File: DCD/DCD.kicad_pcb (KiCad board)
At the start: 4 copper layers, 110 x 110 mm, 172 parts, among them IC1 830S21AMI-01LF, IC2 830S21AMI-01LF, J1 UMPS-04-03.5-G-VT-SM-WT, J2 UMPS-04-03.5-G-VT-SM-WT, J3 UMPS-04-03.5-G-VT-SM-WT, J4 UMPS-04-03.5-G-VT-SM-WT, J5 Conn_02x04_Top_Bottom, U1 TLV76780DBVR, U10 OPA277UA, U11 DAC8811ICDGKT, U12 DAC8811ICDGKT, U13 OPA277UA, U14 OPA277UA, U15 MC100EP31DTG, U16 MC100EP31DTG, U2 ADP7182AUJZ-1.8-R7, U3 LP2985-50DBVR, U4 LP2985-18DBVR, U5 LP2985-33DBVR, U6 ADR4550BRZ, U7 LP2985-33DBVR, U8 CDCLVC1104PWR, U9 AD4630-24BBCZ, Y1 SiT8208AI-21-33E-50.000000

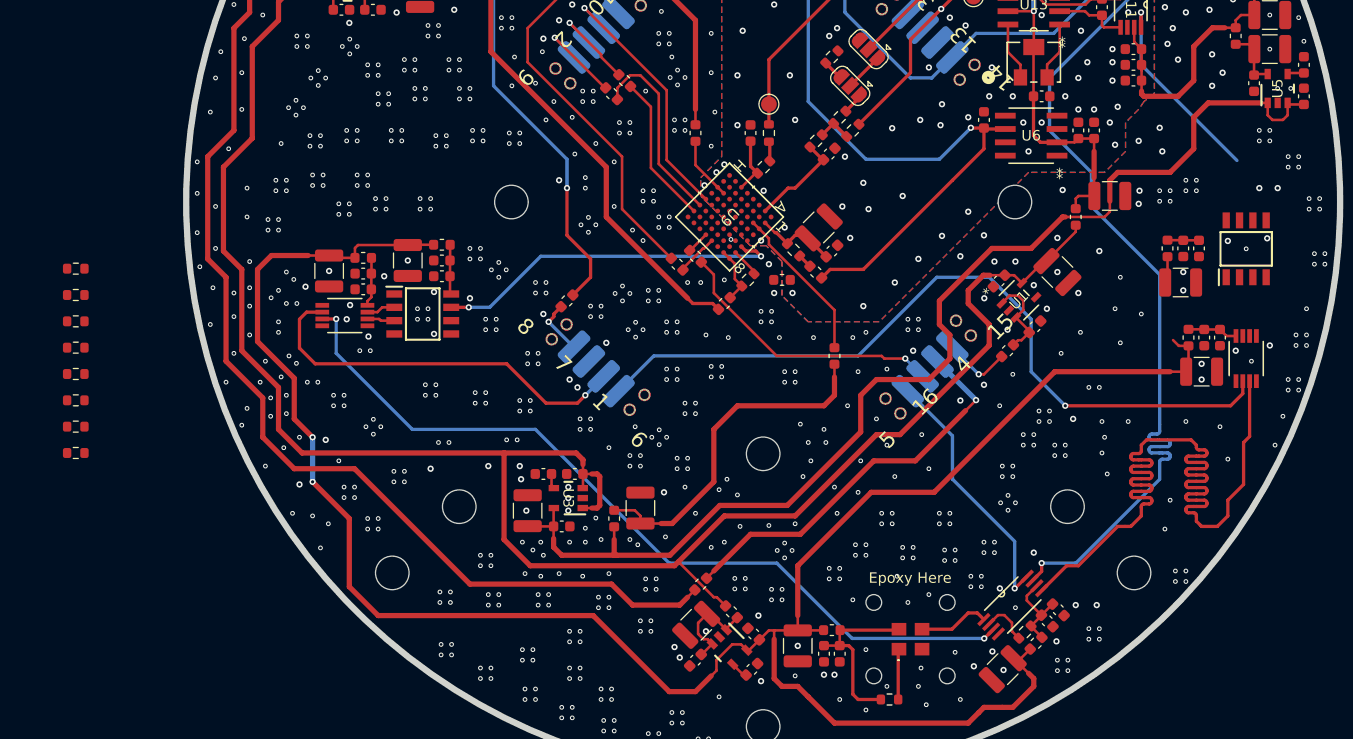
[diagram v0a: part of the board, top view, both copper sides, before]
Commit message: Added components part numbers and stuff. Added termination resistors
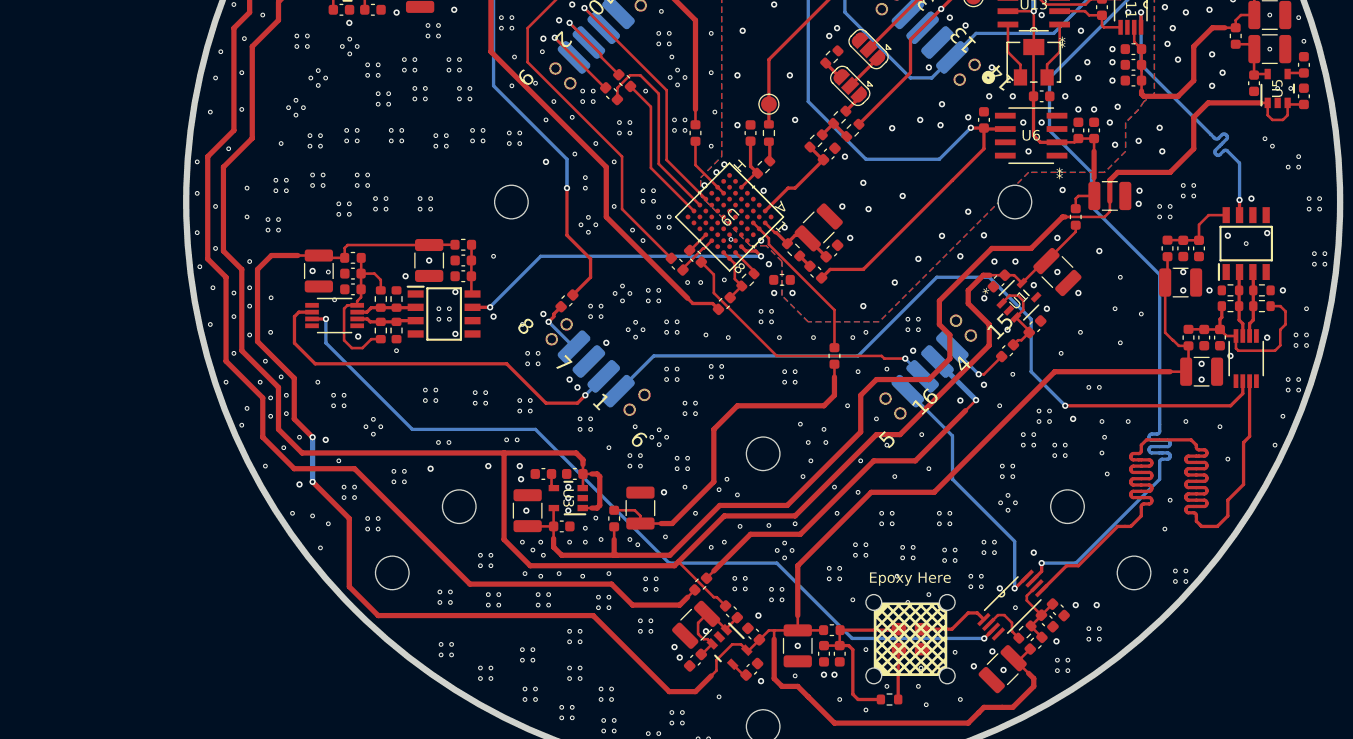
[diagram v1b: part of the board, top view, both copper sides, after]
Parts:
- moved R6 113.1 mm to (194.2, 105.0)
- moved R7 113.1 mm to (194.2, 103.5), turned to 180 degrees
- moved R9 110.2 mm to (191.2, 103.5)
- moved R8 110.1 mm to (191.2, 105.0), turned to 180 degrees
- moved R22 33.9 mm to (111.8, 104.3), turned to -90 degrees
- moved R21 31.5 mm to (110.2, 104.3), turned to 90 degrees
- moved R13 31.3 mm to (111.8, 107.3), turned to 90 degrees
- moved R12 29.4 mm to (110.2, 107.3), turned to -90 degrees
- moved C67 2.04 mm to (118.1, 102.2)
- moved C68 2.04 mm to (118.1, 100.7)
- moved C69 2.04 mm to (114.9, 100.7)
- moved FB29 2.04 mm to (118.1, 99.2)
- moved IC2 2.04 mm to (116.3, 105.8)
- moved C64 0.98 mm to (104.3, 101.7)
- moved C65 0.98 mm to (107.6, 101.9)
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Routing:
- net Net-(U15-VCC): track 4.79 -> 17.9 mm
- net Net-(U16-VCC): track 4.68 -> 16.4 mm
- net /Comms/*CS1: track 19.3 -> 28.0 mm
- net 3V3_CLK: track 200.8 -> 208.7 mm
- net Net-(IC1-NCLK): track 0.08 -> 6.34 mm
- net Net-(IC1-CLK): track 0.00 -> 6.26 mm
- net Net-(IC1-VDD): track 3.27 -> 7.72 mm
- net Net-(IC2-NCLK): track 2.63 -> 5.74 mm
- net Net-(IC2-CLK): track 2.75 -> 5.77 mm
- net /ADC/CNV: track 33.8 -> 31.8 mm
- net /ADC/DGND: vias 945 -> 918

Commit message: Component placement
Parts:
- removed B1: DIN933 M3x14mm, custom_components:Screw_DIN933_M3x14mm
- removed C38: 1µF, Capacitor_SMD:C_0603_1608Metric
- removed C40: 100p, Capacitor_SMD:C_0603_1608Metric
- removed C43: 1nF, Capacitor_SMD:C_0603_1608Metric
- removed C44: 10pF, Capacitor_SMD:C_0603_1608Metric
- removed C47, C48: 100nF, Capacitor_SMD:C_0603_1608Metric
- removed FB11, FB12, FB14: 470Ω, Inductor_SMD:L_0603_1608Metric
- removed H1, H10, H11, H12, H13, H14, H2, H3, H4, H5, H6, H7, H8, H9: M3 Mounting hole, LOBSTER:MountingHole_3.2mm_M3_NoMask
- removed H15: Spacer M3x5mm, custom_components:ThreadedSpacer_6mm_M3x0.5_5mm
- removed J1, J2, J3, J4: UMPS-04-03.5-G-VT-SM-WT, custom_components:UMPS-04-03.5-G-VT-SM-WT
- removed J5: Conn_02x04_Top_Bottom, Connector_PinHeader_2.54mm:PinHeader_2x04_P2.54mm_Vertical
- removed JP1, JP2: SolderJumper_3_Open, Jumper:SolderJumper-3_P1.3mm_Open_RoundedPad1.0x1.5mm
- removed N1, N2, N3, N4, N5, N6, N7: M3 Thumbnut, custom_components:ThumbNut-M3
- removed R17: 47, Resistor_SMD:R_0603_1608Metric
- removed R18, R19, R20: 1k, Resistor_SMD:R_0603_1608Metric
- removed R3, R4, R5: 10k, Resistor_SMD:R_0603_1608Metric
- removed RV1, RV2, RV3: 20kR, custom_components:IC3_3214W-1-203E_BRN
- removed TP1, TP2: TestPoint, TestPoint:TestPoint_Pad_D1.5mm
- removed U11: DAC8811ICDGKT, custom_components:DGK8
- removed U13: OPA277UA, custom_components:D8
- added C23: 10uF, Capacitor_SMD:C_1210_3225Metric, F.Cu at (194.5, 47.6)
- added C23: 10uF, Capacitor_SMD:C_1210_3225Metric, F.Cu at (138.7, 78.9)
- added C23: 10uF, Capacitor_SMD:C_1210_3225Metric, F.Cu at (122.5, 46.9)
- added C23: 10uF, Capacitor_SMD:C_1210_3225Metric, F.Cu at (152.9, 79.4)
- added C23: 10uF, Capacitor_SMD:C_1210_3225Metric, F.Cu at (123.7, 77.9)
- added C23: 10uF, Capacitor_SMD:C_1210_3225Metric, F.Cu at (107.9, 79.2)
- added C23: 10uF, Capacitor_SMD:C_1210_3225Metric, F.Cu at (90.9, 79.4)
- added C23: 10uF, Capacitor_SMD:C_1210_3225Metric, F.Cu at (180.5, 47.9)
- added C23: 10uF, Capacitor_SMD:C_1210_3225Metric, F.Cu at (137.3, 46.9)
- added C23: 10uF, Capacitor_SMD:C_1210_3225Metric, F.Cu at (167.2, 79.7)
- added C23: 10uF, Capacitor_SMD:C_1210_3225Metric, F.Cu at (181.9, 79.7)
- added C23: 10uF, Capacitor_SMD:C_1210_3225Metric, F.Cu at (196.2, 79.7)
- added C23: 10uF, Capacitor_SMD:C_1210_3225Metric, F.Cu at (107.3, 46.4)
- added C23: 10uF, Capacitor_SMD:C_1210_3225Metric, F.Cu at (166.0, 47.6)
- added C23: 10uF, Capacitor_SMD:C_1210_3225Metric, F.Cu at (151.5, 47.9)
- added C30: 10uF, Capacitor_SMD:C_1210_3225Metric, B.Cu at (129.0, 51.5)
- added C30: 10uF, Capacitor_SMD:C_1210_3225Metric, B.Cu at (129.7, 21.9)
- added C30: 10uF, Capacitor_SMD:C_1210_3225Metric, B.Cu at (102.0, 22.7)
- added C30: 10uF, Capacitor_SMD:C_1210_3225Metric, B.Cu at (156.5, 21.4)
- added C30: 10uF, Capacitor_SMD:C_1210_3225Metric, B.Cu at (102.0, 52.0)
- added C30: 10uF, Capacitor_SMD:C_1210_3225Metric, B.Cu at (156.7, 50.0)
- added C30: 10uF, Capacitor_SMD:C_1210_3225Metric, B.Cu at (182.7, 49.0)
- added C32: 100nF, Capacitor_SMD:C_0603_1608Metric, B.Cu at (180.3, 49.8)
- added C32: 100nF, Capacitor_SMD:C_0603_1608Metric, B.Cu at (154.3, 50.8)
- added C32: 100nF, Capacitor_SMD:C_0603_1608Metric, B.Cu at (99.5, 52.8)
- added C32: 100nF, Capacitor_SMD:C_0603_1608Metric, B.Cu at (154.0, 22.2)
- added C32: 100nF, Capacitor_SMD:C_0603_1608Metric, B.Cu at (126.5, 52.2)
- added C32: 100nF, Capacitor_SMD:C_0603_1608Metric, B.Cu at (99.5, 23.4)
- added C32: 100nF, Capacitor_SMD:C_0603_1608Metric, B.Cu at (127.3, 22.7)
- added C36: 1nF, Capacitor_SMD:C_0603_1608Metric, B.Cu at (160.7, 19.7)
- added C36: 1nF, Capacitor_SMD:C_0603_1608Metric, B.Cu at (161.0, 48.3)
- added C36: 1nF, Capacitor_SMD:C_0603_1608Metric, B.Cu at (187.0, 47.3)
- added C36: 1nF, Capacitor_SMD:C_0603_1608Metric, B.Cu at (106.2, 50.3)
- added C36: 1nF, Capacitor_SMD:C_0603_1608Metric, B.Cu at (133.2, 49.8)
- added C36: 1nF, Capacitor_SMD:C_0603_1608Metric, B.Cu at (106.2, 20.9)
- added C36: 1nF, Capacitor_SMD:C_0603_1608Metric, B.Cu at (134.0, 20.2)
- added C37: 1nF, Capacitor_SMD:C_0603_1608Metric, B.Cu at (140.7, 20.2)
- added C37: 1nF, Capacitor_SMD:C_0603_1608Metric, B.Cu at (167.4, 19.7)
- added C37: 1nF, Capacitor_SMD:C_0603_1608Metric, B.Cu at (112.9, 50.3)
- added C37: 1nF, Capacitor_SMD:C_0603_1608Metric, B.Cu at (167.7, 48.3)
- added C37: 1nF, Capacitor_SMD:C_0603_1608Metric, B.Cu at (139.9, 49.8)
- added C37: 1nF, Capacitor_SMD:C_0603_1608Metric, B.Cu at (112.9, 20.9)
- added C37: 1nF, Capacitor_SMD:C_0603_1608Metric, B.Cu at (193.7, 47.3)
- added C39: 1µF, Capacitor_SMD:C_0603_1608Metric, F.Cu at (201.2, 62.8)
- added C39: 1µF, Capacitor_SMD:C_0603_1608Metric, F.Cu at (112.9, 62.2)
- added C39: 1µF, Capacitor_SMD:C_0603_1608Metric, F.Cu at (156.5, 31.0)
- added C39: 1µF, Capacitor_SMD:C_0603_1608Metric, F.Cu at (95.9, 62.5)
- added C39: 1µF, Capacitor_SMD:C_0603_1608Metric, F.Cu at (143.7, 62.0)
- added C39: 1µF, Capacitor_SMD:C_0603_1608Metric, F.Cu at (127.5, 30.0)
- added C39: 1µF, Capacitor_SMD:C_0603_1608Metric, F.Cu at (157.9, 62.5)
- added C39: 1µF, Capacitor_SMD:C_0603_1608Metric, F.Cu at (172.2, 62.7)
- added C39: 1µF, Capacitor_SMD:C_0603_1608Metric, F.Cu at (128.7, 61.0)
- added C39: 1µF, Capacitor_SMD:C_0603_1608Metric, F.Cu at (171.0, 30.7)
- added C39: 1µF, Capacitor_SMD:C_0603_1608Metric, F.Cu at (112.3, 29.5)
- added C39: 1µF, Capacitor_SMD:C_0603_1608Metric, F.Cu at (199.5, 30.7)
- added C39: 1µF, Capacitor_SMD:C_0603_1608Metric, F.Cu at (142.3, 30.0)
- added C39: 1µF, Capacitor_SMD:C_0603_1608Metric, F.Cu at (186.9, 62.7)
- added C39: 1µF, Capacitor_SMD:C_0603_1608Metric, F.Cu at (185.5, 31.0)
- added C41: 100p, Capacitor_SMD:C_0603_1608Metric, F.Cu at (112.3, 26.5)
- added C41: 100p, Capacitor_SMD:C_0603_1608Metric, F.Cu at (143.7, 59.0)
- added C41: 100p, Capacitor_SMD:C_0603_1608Metric, F.Cu at (142.3, 27.0)
- added C41: 100p, Capacitor_SMD:C_0603_1608Metric, F.Cu at (156.5, 28.0)
- added C41: 100p, Capacitor_SMD:C_0603_1608Metric, F.Cu at (157.9, 59.5)
- added C41: 100p, Capacitor_SMD:C_0603_1608Metric, F.Cu at (128.7, 58.0)
- added C41: 100p, Capacitor_SMD:C_0603_1608Metric, F.Cu at (186.9, 59.7)
- added C41: 100p, Capacitor_SMD:C_0603_1608Metric, F.Cu at (171.0, 27.7)
- added C41: 100p, Capacitor_SMD:C_0603_1608Metric, F.Cu at (112.9, 59.2)
- added C41: 100p, Capacitor_SMD:C_0603_1608Metric, F.Cu at (95.9, 59.5)
- added C41: 100p, Capacitor_SMD:C_0603_1608Metric, F.Cu at (201.2, 59.8)
- added C41: 100p, Capacitor_SMD:C_0603_1608Metric, F.Cu at (172.2, 59.7)
- added C41: 100p, Capacitor_SMD:C_0603_1608Metric, F.Cu at (127.5, 27.0)
- added C41: 100p, Capacitor_SMD:C_0603_1608Metric, F.Cu at (199.5, 27.7)
- added C41: 100p, Capacitor_SMD:C_0603_1608Metric, F.Cu at (185.5, 28.0)
- added C42: 1nF, Capacitor_SMD:C_0603_1608Metric, F.Cu at (199.5, 29.2)
- added C42: 1nF, Capacitor_SMD:C_0603_1608Metric, F.Cu at (128.7, 59.5)
- added C42: 1nF, Capacitor_SMD:C_0603_1608Metric, F.Cu at (185.5, 29.5)
- added C42: 1nF, Capacitor_SMD:C_0603_1608Metric, F.Cu at (95.9, 61.0)
- added C42: 1nF, Capacitor_SMD:C_0603_1608Metric, F.Cu at (201.2, 61.3)
- added C42: 1nF, Capacitor_SMD:C_0603_1608Metric, F.Cu at (143.7, 60.5)
- added C42: 1nF, Capacitor_SMD:C_0603_1608Metric, F.Cu at (112.9, 60.7)
- added C42: 1nF, Capacitor_SMD:C_0603_1608Metric, F.Cu at (172.2, 61.2)
- added C42: 1nF, Capacitor_SMD:C_0603_1608Metric, F.Cu at (171.0, 29.2)
- added C42: 1nF, Capacitor_SMD:C_0603_1608Metric, F.Cu at (157.9, 61.0)
- added C42: 1nF, Capacitor_SMD:C_0603_1608Metric, F.Cu at (156.5, 29.5)
- added C42: 1nF, Capacitor_SMD:C_0603_1608Metric, F.Cu at (142.3, 28.5)
- added C42: 1nF, Capacitor_SMD:C_0603_1608Metric, F.Cu at (127.5, 28.5)
- added C42: 1nF, Capacitor_SMD:C_0603_1608Metric, F.Cu at (112.3, 28.0)
- added C42: 1nF, Capacitor_SMD:C_0603_1608Metric, F.Cu at (186.9, 61.2)
- added C45: 10pF, Capacitor_SMD:C_0603_1608Metric, F.Cu at (196.6, 23.2)
- added C45: 10pF, Capacitor_SMD:C_0603_1608Metric, F.Cu at (109.3, 22.0)
- added C45: 10pF, Capacitor_SMD:C_0603_1608Metric, F.Cu at (124.6, 22.5)
- added C45: 10pF, Capacitor_SMD:C_0603_1608Metric, F.Cu at (125.7, 53.5)
- added C45: 10pF, Capacitor_SMD:C_0603_1608Metric, F.Cu at (93.0, 55.0)
- added C45: 10pF, Capacitor_SMD:C_0603_1608Metric, F.Cu at (155.0, 55.0)
- added C45: 10pF, Capacitor_SMD:C_0603_1608Metric, F.Cu at (139.3, 22.5)
- added C45: 10pF, Capacitor_SMD:C_0603_1608Metric, F.Cu at (184.0, 55.2)
- added C45: 10pF, Capacitor_SMD:C_0603_1608Metric, F.Cu at (169.2, 55.2)
- added C45: 10pF, Capacitor_SMD:C_0603_1608Metric, F.Cu at (140.7, 54.5)
- added C45: 10pF, Capacitor_SMD:C_0603_1608Metric, F.Cu at (182.6, 23.5)
- added C45: 10pF, Capacitor_SMD:C_0603_1608Metric, F.Cu at (110.0, 54.7)
- added C45: 10pF, Capacitor_SMD:C_0603_1608Metric, F.Cu at (153.6, 23.5)
- added C45: 10pF, Capacitor_SMD:C_0603_1608Metric, F.Cu at (198.2, 55.3)
- added C45: 10pF, Capacitor_SMD:C_0603_1608Metric, F.Cu at (168.1, 23.2)
- added C49: 100nF, Capacitor_SMD:C_0603_1608Metric, F.Cu at (141.2, 50.5)
- added C49: 100nF, Capacitor_SMD:C_0603_1608Metric, F.Cu at (109.8, 18.0)
- added C49: 100nF, Capacitor_SMD:C_0603_1608Metric, F.Cu at (169.7, 51.2)
- added C49: 100nF, Capacitor_SMD:C_0603_1608Metric, F.Cu at (168.5, 19.2)
- added C49: 100nF, Capacitor_SMD:C_0603_1608Metric, F.Cu at (198.7, 51.3)
- added C49: 100nF, Capacitor_SMD:C_0603_1608Metric, F.Cu at (197.0, 19.2)
- added C49: 100nF, Capacitor_SMD:C_0603_1608Metric, F.Cu at (125.0, 18.5)
- added C49: 100nF, Capacitor_SMD:C_0603_1608Metric, F.Cu at (154.0, 19.5)
- added C49: 100nF, Capacitor_SMD:C_0603_1608Metric, F.Cu at (184.4, 51.2)
- added C49: 100nF, Capacitor_SMD:C_0603_1608Metric, F.Cu at (155.4, 51.0)
- added C49: 100nF, Capacitor_SMD:C_0603_1608Metric, F.Cu at (139.8, 18.5)
- added C49: 100nF, Capacitor_SMD:C_0603_1608Metric, F.Cu at (93.4, 51.0)
- added C49: 100nF, Capacitor_SMD:C_0603_1608Metric, F.Cu at (183.0, 19.5)
- added C49: 100nF, Capacitor_SMD:C_0603_1608Metric, F.Cu at (110.4, 50.7)
- added C50: 100nF, Capacitor_SMD:C_0603_1608Metric, F.Cu at (181.6, 28.7)
- added C50: 100nF, Capacitor_SMD:C_0603_1608Metric, F.Cu at (109.0, 60.0)
- added C50: 100nF, Capacitor_SMD:C_0603_1608Metric, F.Cu at (168.2, 60.5)
- added C50: 100nF, Capacitor_SMD:C_0603_1608Metric, F.Cu at (197.2, 60.5)
- added C50: 100nF, Capacitor_SMD:C_0603_1608Metric, F.Cu at (139.7, 59.7)
- added C50: 100nF, Capacitor_SMD:C_0603_1608Metric, F.Cu at (183.0, 60.5)
- added C50: 100nF, Capacitor_SMD:C_0603_1608Metric, F.Cu at (92.0, 60.2)
- added C50: 100nF, Capacitor_SMD:C_0603_1608Metric, F.Cu at (154.0, 60.2)
- added C50: 100nF, Capacitor_SMD:C_0603_1608Metric, F.Cu at (108.3, 27.2)
- added C50: 100nF, Capacitor_SMD:C_0603_1608Metric, F.Cu at (138.3, 27.7)
- added C50: 100nF, Capacitor_SMD:C_0603_1608Metric, F.Cu at (123.6, 27.7)
- added C50: 100nF, Capacitor_SMD:C_0603_1608Metric, F.Cu at (167.1, 28.5)
- added C50: 100nF, Capacitor_SMD:C_0603_1608Metric, F.Cu at (195.6, 28.5)
- added C50: 100nF, Capacitor_SMD:C_0603_1608Metric, F.Cu at (124.7, 58.7)
- added C50: 100nF, Capacitor_SMD:C_0603_1608Metric, F.Cu at (152.6, 28.7)
- added C59: 1µF, Capacitor_SMD:C_0603_1608Metric, F.Cu at (138.9, 75.7)
- added C59: 1µF, Capacitor_SMD:C_0603_1608Metric, F.Cu at (182.2, 76.4)
- added C59: 1µF, Capacitor_SMD:C_0603_1608Metric, F.Cu at (167.4, 76.4)
- added C59: 1µF, Capacitor_SMD:C_0603_1608Metric, F.Cu at (151.8, 44.6)
- added C59: 1µF, Capacitor_SMD:C_0603_1608Metric, F.Cu at (180.8, 44.6)
- added C59: 1µF, Capacitor_SMD:C_0603_1608Metric, F.Cu at (108.2, 75.9)
- added C59: 1µF, Capacitor_SMD:C_0603_1608Metric, F.Cu at (137.5, 43.6)
- added C59: 1µF, Capacitor_SMD:C_0603_1608Metric, F.Cu at (153.2, 76.2)
- added C59: 1µF, Capacitor_SMD:C_0603_1608Metric, F.Cu at (123.9, 74.7)
- added C59: 1µF, Capacitor_SMD:C_0603_1608Metric, F.Cu at (91.2, 76.2)
- added C59: 1µF, Capacitor_SMD:C_0603_1608Metric, F.Cu at (194.8, 44.4)
- added C59: 1µF, Capacitor_SMD:C_0603_1608Metric, F.Cu at (107.5, 43.1)
- added C59: 1µF, Capacitor_SMD:C_0603_1608Metric, F.Cu at (122.8, 43.6)
- added C59: 1µF, Capacitor_SMD:C_0603_1608Metric, F.Cu at (196.4, 76.4)
- added C59: 1µF, Capacitor_SMD:C_0603_1608Metric, F.Cu at (166.3, 44.4)
- added C60: 100nF, Capacitor_SMD:C_0603_1608Metric, F.Cu at (153.3, 44.6)
- added C60: 100nF, Capacitor_SMD:C_0603_1608Metric, F.Cu at (92.7, 76.2)
- added C60: 100nF, Capacitor_SMD:C_0603_1608Metric, F.Cu at (167.8, 44.4)
- added C60: 100nF, Capacitor_SMD:C_0603_1608Metric, F.Cu at (109.0, 43.1)
- added C60: 100nF, Capacitor_SMD:C_0603_1608Metric, F.Cu at (139.0, 43.6)
- added C60: 100nF, Capacitor_SMD:C_0603_1608Metric, F.Cu at (109.7, 75.9)
- added C60: 100nF, Capacitor_SMD:C_0603_1608Metric, F.Cu at (140.4, 75.7)
- added C60: 100nF, Capacitor_SMD:C_0603_1608Metric, F.Cu at (124.3, 43.6)
- added C60: 100nF, Capacitor_SMD:C_0603_1608Metric, F.Cu at (183.7, 76.4)
- added C60: 100nF, Capacitor_SMD:C_0603_1608Metric, F.Cu at (154.7, 76.2)
- added C60: 100nF, Capacitor_SMD:C_0603_1608Metric, F.Cu at (197.9, 76.4)
- added C60: 100nF, Capacitor_SMD:C_0603_1608Metric, F.Cu at (168.9, 76.4)
- added C60: 100nF, Capacitor_SMD:C_0603_1608Metric, F.Cu at (196.3, 44.4)
- added C60: 100nF, Capacitor_SMD:C_0603_1608Metric, F.Cu at (125.4, 74.7)
- added C60: 100nF, Capacitor_SMD:C_0603_1608Metric, F.Cu at (182.3, 44.6)
- added C61: 10uF, Capacitor_SMD:C_1210_3225Metric, F.Cu at (136.7, 70.4)
- added C61: 10uF, Capacitor_SMD:C_1210_3225Metric, F.Cu at (120.5, 38.4)
- added C61: 10uF, Capacitor_SMD:C_1210_3225Metric, F.Cu at (149.5, 39.4)
- added C61: 10uF, Capacitor_SMD:C_1210_3225Metric, F.Cu at (88.9, 70.9)
- added C61: 10uF, Capacitor_SMD:C_1210_3225Metric, F.Cu at (121.7, 69.4)
- added C61: 10uF, Capacitor_SMD:C_1210_3225Metric, F.Cu at (178.5, 39.4)
- added C61: 10uF, Capacitor_SMD:C_1210_3225Metric, F.Cu at (135.3, 38.4)
- added C61: 10uF, Capacitor_SMD:C_1210_3225Metric, F.Cu at (165.2, 71.2)
- added C61: 10uF, Capacitor_SMD:C_1210_3225Metric, F.Cu at (105.3, 37.9)
- added C61: 10uF, Capacitor_SMD:C_1210_3225Metric, F.Cu at (179.9, 71.2)
- added C61: 10uF, Capacitor_SMD:C_1210_3225Metric, F.Cu at (150.9, 70.9)
- added C61: 10uF, Capacitor_SMD:C_1210_3225Metric, F.Cu at (105.9, 70.7)
- added C61: 10uF, Capacitor_SMD:C_1210_3225Metric, F.Cu at (164.0, 39.1)
- added C61: 10uF, Capacitor_SMD:C_1210_3225Metric, F.Cu at (194.2, 71.2)
- added C61: 10uF, Capacitor_SMD:C_1210_3225Metric, F.Cu at (192.5, 39.1)
- added C62: 1µF, Capacitor_SMD:C_0603_1608Metric, F.Cu at (151.2, 67.7)
- added C62: 1µF, Capacitor_SMD:C_0603_1608Metric, F.Cu at (105.5, 34.6)
- added C62: 1µF, Capacitor_SMD:C_0603_1608Metric, F.Cu at (120.8, 35.1)
- added C62: 1µF, Capacitor_SMD:C_0603_1608Metric, F.Cu at (89.2, 67.7)
- added C62: 1µF, Capacitor_SMD:C_0603_1608Metric, F.Cu at (165.4, 67.9)
- added C62: 1µF, Capacitor_SMD:C_0603_1608Metric, F.Cu at (192.8, 35.9)
- added C62: 1µF, Capacitor_SMD:C_0603_1608Metric, F.Cu at (194.4, 67.9)
- added C62: 1µF, Capacitor_SMD:C_0603_1608Metric, F.Cu at (178.8, 36.1)
- added C62: 1µF, Capacitor_SMD:C_0603_1608Metric, F.Cu at (106.2, 67.4)
- added C62: 1µF, Capacitor_SMD:C_0603_1608Metric, F.Cu at (121.9, 66.2)
- added C62: 1µF, Capacitor_SMD:C_0603_1608Metric, F.Cu at (135.5, 35.1)
- added C62: 1µF, Capacitor_SMD:C_0603_1608Metric, F.Cu at (149.8, 36.1)
- added C62: 1µF, Capacitor_SMD:C_0603_1608Metric, F.Cu at (164.3, 35.9)
- added C62: 1µF, Capacitor_SMD:C_0603_1608Metric, F.Cu at (180.2, 67.9)
- added C62: 1µF, Capacitor_SMD:C_0603_1608Metric, F.Cu at (136.9, 67.2)
- added C63: 100nF, Capacitor_SMD:C_0603_1608Metric, F.Cu at (180.3, 36.1)
- added C63: 100nF, Capacitor_SMD:C_0603_1608Metric, F.Cu at (166.9, 67.9)
- added C63: 100nF, Capacitor_SMD:C_0603_1608Metric, F.Cu at (107.0, 34.6)
- added C63: 100nF, Capacitor_SMD:C_0603_1608Metric, F.Cu at (138.4, 67.2)
- added C63: 100nF, Capacitor_SMD:C_0603_1608Metric, F.Cu at (165.8, 35.9)
- added C63: 100nF, Capacitor_SMD:C_0603_1608Metric, F.Cu at (194.3, 35.9)
- added C63: 100nF, Capacitor_SMD:C_0603_1608Metric, F.Cu at (123.4, 66.2)
- added C63: 100nF, Capacitor_SMD:C_0603_1608Metric, F.Cu at (195.9, 67.9)
- added C63: 100nF, Capacitor_SMD:C_0603_1608Metric, F.Cu at (181.7, 67.9)
- added C63: 100nF, Capacitor_SMD:C_0603_1608Metric, F.Cu at (90.7, 67.7)
- added C63: 100nF, Capacitor_SMD:C_0603_1608Metric, F.Cu at (137.0, 35.1)
- added C63: 100nF, Capacitor_SMD:C_0603_1608Metric, F.Cu at (151.3, 36.1)
- added C63: 100nF, Capacitor_SMD:C_0603_1608Metric, F.Cu at (107.7, 67.4)
- added C63: 100nF, Capacitor_SMD:C_0603_1608Metric, F.Cu at (152.7, 67.7)
- added C63: 100nF, Capacitor_SMD:C_0603_1608Metric, F.Cu at (122.3, 35.1)
- added C64: 10uF, Capacitor_SMD:C_1210_3225Metric, B.Cu at (168.4, 38.7)
- added C64: 10uF, Capacitor_SMD:C_1210_3225Metric, B.Cu at (141.6, 39.2)
- added C64: 10uF, Capacitor_SMD:C_1210_3225Metric, B.Cu at (168.6, 67.3)
- added C64: 10uF, Capacitor_SMD:C_1210_3225Metric, B.Cu at (113.9, 69.3)
- added C64: 10uF, Capacitor_SMD:C_1210_3225Metric, B.Cu at (113.9, 39.9)
- added C64: 10uF, Capacitor_SMD:C_1210_3225Metric, B.Cu at (140.9, 68.8)
- added C64: 10uF, Capacitor_SMD:C_1210_3225Metric, B.Cu at (194.6, 66.3)
- added C65: 1µF, Capacitor_SMD:C_0603_1608Metric, B.Cu at (110.6, 40.2)
- added C65: 1µF, Capacitor_SMD:C_0603_1608Metric, B.Cu at (138.4, 39.4)
- added C65: 1µF, Capacitor_SMD:C_0603_1608Metric, B.Cu at (191.4, 66.5)
- added C65: 1µF, Capacitor_SMD:C_0603_1608Metric, B.Cu at (137.6, 69.0)
- added C65: 1µF, Capacitor_SMD:C_0603_1608Metric, B.Cu at (165.4, 67.5)
- added C65: 1µF, Capacitor_SMD:C_0603_1608Metric, B.Cu at (110.6, 69.5)
- added C65: 1µF, Capacitor_SMD:C_0603_1608Metric, B.Cu at (165.1, 38.9)
- added C66: 100nF, Capacitor_SMD:C_0603_1608Metric, B.Cu at (138.4, 40.9)
- added C66: 100nF, Capacitor_SMD:C_0603_1608Metric, B.Cu at (165.4, 69.0)
- added C66: 100nF, Capacitor_SMD:C_0603_1608Metric, B.Cu at (110.6, 71.0)
- added C66: 100nF, Capacitor_SMD:C_0603_1608Metric, B.Cu at (137.6, 70.5)
- added C66: 100nF, Capacitor_SMD:C_0603_1608Metric, B.Cu at (191.4, 68.0)
- added C66: 100nF, Capacitor_SMD:C_0603_1608Metric, B.Cu at (165.1, 40.4)
- added C66: 100nF, Capacitor_SMD:C_0603_1608Metric, B.Cu at (110.6, 41.7)
- added C67: 100nF, Capacitor_SMD:C_0603_1608Metric, B.Cu at (180.9, 66.8)
- added C67: 100nF, Capacitor_SMD:C_0603_1608Metric, B.Cu at (100.1, 69.8)
- added C67: 100nF, Capacitor_SMD:C_0603_1608Metric, B.Cu at (154.9, 67.8)
- added C67: 100nF, Capacitor_SMD:C_0603_1608Metric, B.Cu at (154.6, 39.2)
- added C67: 100nF, Capacitor_SMD:C_0603_1608Metric, B.Cu at (127.9, 39.7)
- added C67: 100nF, Capacitor_SMD:C_0603_1608Metric, B.Cu at (127.1, 69.3)
- added C67: 100nF, Capacitor_SMD:C_0603_1608Metric, B.Cu at (100.1, 40.4)
- added C68: 1µF, Capacitor_SMD:C_0603_1608Metric, B.Cu at (180.9, 65.3)
- added C68: 1µF, Capacitor_SMD:C_0603_1608Metric, B.Cu at (100.1, 38.9)
- added C68: 1µF, Capacitor_SMD:C_0603_1608Metric, B.Cu at (127.1, 67.8)
- added C68: 1µF, Capacitor_SMD:C_0603_1608Metric, B.Cu at (154.9, 66.3)
- added C68: 1µF, Capacitor_SMD:C_0603_1608Metric, B.Cu at (100.1, 68.3)
- added C68: 1µF, Capacitor_SMD:C_0603_1608Metric, B.Cu at (154.6, 37.7)
- added C68: 1µF, Capacitor_SMD:C_0603_1608Metric, B.Cu at (127.9, 38.2)
- added C69: 10uF, Capacitor_SMD:C_1210_3225Metric, B.Cu at (157.9, 37.7)
- added C69: 10uF, Capacitor_SMD:C_1210_3225Metric, B.Cu at (158.1, 66.3)
- added C69: 10uF, Capacitor_SMD:C_1210_3225Metric, B.Cu at (103.4, 38.9)
- added C69: 10uF, Capacitor_SMD:C_1210_3225Metric, B.Cu at (131.1, 38.2)
- added C69: 10uF, Capacitor_SMD:C_1210_3225Metric, B.Cu at (103.4, 68.3)
- added C69: 10uF, Capacitor_SMD:C_1210_3225Metric, B.Cu at (184.1, 65.3)
- added C69: 10uF, Capacitor_SMD:C_1210_3225Metric, B.Cu at (130.4, 67.8)
- added FB10: 470Ω, Inductor_SMD:L_0603_1608Metric, B.Cu at (136.1, 32.2)
- added FB10: 470Ω, Inductor_SMD:L_0603_1608Metric, B.Cu at (108.3, 32.9)
- added FB10: 470Ω, Inductor_SMD:L_0603_1608Metric, B.Cu at (163.1, 60.3)
- added FB10: 470Ω, Inductor_SMD:L_0603_1608Metric, B.Cu at (189.1, 59.3)
- added FB10: 470Ω, Inductor_SMD:L_0603_1608Metric, B.Cu at (162.8, 31.7)
- added FB10: 470Ω, Inductor_SMD:L_0603_1608Metric, B.Cu at (108.3, 62.3)
- added FB10: 470Ω, Inductor_SMD:L_0603_1608Metric, B.Cu at (135.3, 61.8)
- added FB13: 470Ω, Inductor_SMD:L_0603_1608Metric, B.Cu at (115.2, 57.9)
- added FB13: 470Ω, Inductor_SMD:L_0603_1608Metric, B.Cu at (169.9, 55.9)
- added FB13: 470Ω, Inductor_SMD:L_0603_1608Metric, B.Cu at (142.9, 27.8)
- added FB13: 470Ω, Inductor_SMD:L_0603_1608Metric, B.Cu at (195.9, 54.9)
- added FB13: 470Ω, Inductor_SMD:L_0603_1608Metric, B.Cu at (142.2, 57.4)
- added FB13: 470Ω, Inductor_SMD:L_0603_1608Metric, B.Cu at (115.2, 28.5)
- added FB13: 470Ω, Inductor_SMD:L_0603_1608Metric, B.Cu at (169.7, 27.3)
- added FB16: 470Ω, Inductor_SMD:L_0603_1608Metric, B.Cu at (115.2, 59.6)
- added FB16: 470Ω, Inductor_SMD:L_0603_1608Metric, B.Cu at (195.9, 56.6)
- added FB16: 470Ω, Inductor_SMD:L_0603_1608Metric, B.Cu at (169.7, 29.0)
- added FB16: 470Ω, Inductor_SMD:L_0603_1608Metric, B.Cu at (169.9, 57.6)
- added FB16: 470Ω, Inductor_SMD:L_0603_1608Metric, B.Cu at (142.9, 29.5)
- added FB16: 470Ω, Inductor_SMD:L_0603_1608Metric, B.Cu at (115.2, 30.3)
- added FB16: 470Ω, Inductor_SMD:L_0603_1608Metric, B.Cu at (142.2, 59.1)
- added FB20: 470Ω, Inductor_SMD:L_0603_1608Metric, B.Cu at (100.9, 28.7)
- added FB20: 470Ω, Inductor_SMD:L_0603_1608Metric, B.Cu at (181.7, 55.1)
- added FB20: 470Ω, Inductor_SMD:L_0603_1608Metric, B.Cu at (100.9, 58.1)
- added FB20: 470Ω, Inductor_SMD:L_0603_1608Metric, B.Cu at (127.9, 57.6)
- added FB20: 470Ω, Inductor_SMD:L_0603_1608Metric, B.Cu at (155.4, 27.5)
- added FB20: 470Ω, Inductor_SMD:L_0603_1608Metric, B.Cu at (155.7, 56.1)
- added FB20: 470Ω, Inductor_SMD:L_0603_1608Metric, B.Cu at (128.7, 28.0)
- added FB22: 470Ω, Inductor_SMD:L_0603_1608Metric, B.Cu at (103.2, 34.2)
- added FB22: 470Ω, Inductor_SMD:L_0603_1608Metric, B.Cu at (130.2, 63.0)
- added FB22: 470Ω, Inductor_SMD:L_0603_1608Metric, B.Cu at (158.0, 61.5)
- added FB22: 470Ω, Inductor_SMD:L_0603_1608Metric, B.Cu at (184.0, 60.5)
- added FB22: 470Ω, Inductor_SMD:L_0603_1608Metric, B.Cu at (157.7, 32.9)
- added FB22: 470Ω, Inductor_SMD:L_0603_1608Metric, B.Cu at (103.2, 63.5)
- added FB22: 470Ω, Inductor_SMD:L_0603_1608Metric, B.Cu at (131.0, 33.4)
- added FB23: 470Ω, Inductor_SMD:L_0603_1608Metric, B.Cu at (169.7, 52.7)
- added FB23: 470Ω, Inductor_SMD:L_0603_1608Metric, B.Cu at (141.9, 54.2)
- added FB23: 470Ω, Inductor_SMD:L_0603_1608Metric, B.Cu at (114.9, 54.7)
- added FB23: 470Ω, Inductor_SMD:L_0603_1608Metric, B.Cu at (142.7, 24.6)
- added FB23: 470Ω, Inductor_SMD:L_0603_1608Metric, B.Cu at (169.4, 24.1)
- added FB23: 470Ω, Inductor_SMD:L_0603_1608Metric, B.Cu at (114.9, 25.3)
- added FB23: 470Ω, Inductor_SMD:L_0603_1608Metric, B.Cu at (195.7, 51.7)
- added FB24: 470Ω, Inductor_SMD:L_0603_1608Metric, B.Cu at (124.8, 29.4)
- added FB24: 470Ω, Inductor_SMD:L_0603_1608Metric, B.Cu at (177.8, 56.5)
- added FB24: 470Ω, Inductor_SMD:L_0603_1608Metric, B.Cu at (151.5, 28.9)
- added FB24: 470Ω, Inductor_SMD:L_0603_1608Metric, B.Cu at (97.0, 59.5)
- added FB24: 470Ω, Inductor_SMD:L_0603_1608Metric, B.Cu at (97.0, 30.1)
- added FB24: 470Ω, Inductor_SMD:L_0603_1608Metric, B.Cu at (151.8, 57.5)
- added FB24: 470Ω, Inductor_SMD:L_0603_1608Metric, B.Cu at (124.0, 59.0)
- added FB26: 470Ω, Inductor_SMD:L_0603_1608Metric, F.Cu at (151.7, 76.2)
- added FB26: 470Ω, Inductor_SMD:L_0603_1608Metric, F.Cu at (150.3, 44.6)
- added FB26: 470Ω, Inductor_SMD:L_0603_1608Metric, F.Cu at (106.7, 75.9)
- added FB26: 470Ω, Inductor_SMD:L_0603_1608Metric, F.Cu at (136.0, 43.6)
- added FB26: 470Ω, Inductor_SMD:L_0603_1608Metric, F.Cu at (180.7, 76.4)
- added FB26: 470Ω, Inductor_SMD:L_0603_1608Metric, F.Cu at (179.3, 44.6)
- added FB26: 470Ω, Inductor_SMD:L_0603_1608Metric, F.Cu at (122.4, 74.7)
- added FB26: 470Ω, Inductor_SMD:L_0603_1608Metric, F.Cu at (121.3, 43.6)
- added FB26: 470Ω, Inductor_SMD:L_0603_1608Metric, F.Cu at (165.9, 76.4)
- added FB26: 470Ω, Inductor_SMD:L_0603_1608Metric, F.Cu at (137.4, 75.7)
- added FB26: 470Ω, Inductor_SMD:L_0603_1608Metric, F.Cu at (193.3, 44.4)
- added FB26: 470Ω, Inductor_SMD:L_0603_1608Metric, F.Cu at (106.0, 43.1)
- added FB26: 470Ω, Inductor_SMD:L_0603_1608Metric, F.Cu at (89.7, 76.2)
- added FB26: 470Ω, Inductor_SMD:L_0603_1608Metric, F.Cu at (194.9, 76.4)
- added FB26: 470Ω, Inductor_SMD:L_0603_1608Metric, F.Cu at (164.8, 44.4)
- added FB27: 470Ω, Inductor_SMD:L_0603_1608Metric, F.Cu at (87.7, 67.7)
- added FB27: 470Ω, Inductor_SMD:L_0603_1608Metric, F.Cu at (148.3, 36.1)
- added FB27: 470Ω, Inductor_SMD:L_0603_1608Metric, F.Cu at (163.9, 67.9)
- added FB27: 470Ω, Inductor_SMD:L_0603_1608Metric, F.Cu at (104.7, 67.4)
- added FB27: 470Ω, Inductor_SMD:L_0603_1608Metric, F.Cu at (192.9, 67.9)
- added FB27: 470Ω, Inductor_SMD:L_0603_1608Metric, F.Cu at (119.3, 35.1)
- added FB27: 470Ω, Inductor_SMD:L_0603_1608Metric, F.Cu at (134.0, 35.1)
- added FB27: 470Ω, Inductor_SMD:L_0603_1608Metric, F.Cu at (162.8, 35.9)
- added FB27: 470Ω, Inductor_SMD:L_0603_1608Metric, F.Cu at (149.7, 67.7)
- added FB27: 470Ω, Inductor_SMD:L_0603_1608Metric, F.Cu at (120.4, 66.2)
- added FB27: 470Ω, Inductor_SMD:L_0603_1608Metric, F.Cu at (178.7, 67.9)
- added FB27: 470Ω, Inductor_SMD:L_0603_1608Metric, F.Cu at (104.0, 34.6)
- added FB27: 470Ω, Inductor_SMD:L_0603_1608Metric, F.Cu at (177.3, 36.1)
- added FB27: 470Ω, Inductor_SMD:L_0603_1608Metric, F.Cu at (191.3, 35.9)
- added FB27: 470Ω, Inductor_SMD:L_0603_1608Metric, F.Cu at (135.4, 67.2)
- added FB28: 470Ω, Inductor_SMD:L_0603_1608Metric, B.Cu at (110.6, 68.0)
- added FB28: 470Ω, Inductor_SMD:L_0603_1608Metric, B.Cu at (165.1, 37.4)
- added FB28: 470Ω, Inductor_SMD:L_0603_1608Metric, B.Cu at (165.4, 66.0)
- added FB28: 470Ω, Inductor_SMD:L_0603_1608Metric, B.Cu at (137.6, 67.5)
- added FB28: 470Ω, Inductor_SMD:L_0603_1608Metric, B.Cu at (138.4, 37.9)
- added FB28: 470Ω, Inductor_SMD:L_0603_1608Metric, B.Cu at (191.4, 65.0)
- added FB28: 470Ω, Inductor_SMD:L_0603_1608Metric, B.Cu at (110.6, 38.7)
- added FB29: 470Ω, Inductor_SMD:L_0603_1608Metric, B.Cu at (127.1, 66.3)
- added FB29: 470Ω, Inductor_SMD:L_0603_1608Metric, B.Cu at (100.1, 37.4)
- added FB29: 470Ω, Inductor_SMD:L_0603_1608Metric, B.Cu at (180.9, 63.8)
- added FB29: 470Ω, Inductor_SMD:L_0603_1608Metric, B.Cu at (154.6, 36.2)
- added FB29: 470Ω, Inductor_SMD:L_0603_1608Metric, B.Cu at (127.9, 36.7)
- added FB29: 470Ω, Inductor_SMD:L_0603_1608Metric, B.Cu at (100.1, 66.8)
- added FB29: 470Ω, Inductor_SMD:L_0603_1608Metric, B.Cu at (154.9, 64.8)
- added FB7: 470Ω, Inductor_SMD:L_0603_1608Metric, B.Cu at (99.2, 55.2)
- added FB7: 470Ω, Inductor_SMD:L_0603_1608Metric, B.Cu at (153.9, 53.2)
- added FB7: 470Ω, Inductor_SMD:L_0603_1608Metric, B.Cu at (179.9, 52.2)
- added FB7: 470Ω, Inductor_SMD:L_0603_1608Metric, B.Cu at (126.2, 54.8)
- added FB7: 470Ω, Inductor_SMD:L_0603_1608Metric, B.Cu at (153.7, 24.7)
- added FB7: 470Ω, Inductor_SMD:L_0603_1608Metric, B.Cu at (99.2, 25.9)
- added FB7: 470Ω, Inductor_SMD:L_0603_1608Metric, B.Cu at (126.9, 25.2)
- added FB9: 470Ω, Inductor_SMD:L_0603_1608Metric, B.Cu at (189.8, 61.1)
- added FB9: 470Ω, Inductor_SMD:L_0603_1608Metric, B.Cu at (136.8, 34.0)
- added FB9: 470Ω, Inductor_SMD:L_0603_1608Metric, B.Cu at (109.1, 64.1)
- added FB9: 470Ω, Inductor_SMD:L_0603_1608Metric, B.Cu at (109.1, 34.7)
- added FB9: 470Ω, Inductor_SMD:L_0603_1608Metric, B.Cu at (163.6, 33.5)
- added FB9: 470Ω, Inductor_SMD:L_0603_1608Metric, B.Cu at (136.1, 63.6)
- added FB9: 470Ω, Inductor_SMD:L_0603_1608Metric, B.Cu at (163.8, 62.1)
- added IC1: 830S21AMI-01LF, custom_components:SOIC127P600X175-8N, F.Cu at (111.5, 34.2)
- added IC1: 830S21AMI-01LF, custom_components:SOIC127P600X175-8N, F.Cu at (170.3, 35.4)
- added IC1: 830S21AMI-01LF, custom_components:SOIC127P600X175-8N, F.Cu at (184.8, 35.7)
- added IC1: 830S21AMI-01LF, custom_components:SOIC127P600X175-8N, F.Cu at (127.9, 65.7)
- added IC1: 830S21AMI-01LF, custom_components:SOIC127P600X175-8N, F.Cu at (126.8, 34.7)
- added IC1: 830S21AMI-01LF, custom_components:SOIC127P600X175-8N, F.Cu at (186.2, 67.4)
- added IC1: 830S21AMI-01LF, custom_components:SOIC127P600X175-8N, F.Cu at (157.2, 67.2)
- added IC1: 830S21AMI-01LF, custom_components:SOIC127P600X175-8N, F.Cu at (95.2, 67.2)
- added IC1: 830S21AMI-01LF, custom_components:SOIC127P600X175-8N, F.Cu at (198.8, 35.4)
- added IC1: 830S21AMI-01LF, custom_components:SOIC127P600X175-8N, F.Cu at (200.4, 67.5)
- added IC1: 830S21AMI-01LF, custom_components:SOIC127P600X175-8N, F.Cu at (155.8, 35.7)
- added IC1: 830S21AMI-01LF, custom_components:SOIC127P600X175-8N, F.Cu at (171.4, 67.4)
- added IC1: 830S21AMI-01LF, custom_components:SOIC127P600X175-8N, F.Cu at (112.2, 66.9)
- added IC1: 830S21AMI-01LF, custom_components:SOIC127P600X175-8N, F.Cu at (141.5, 34.7)
- added IC1: 830S21AMI-01LF, custom_components:SOIC127P600X175-8N, F.Cu at (142.9, 66.7)
- added IC2: 830S21AMI-01LF, custom_components:SOIC127P600X175-8N, B.Cu at (182.7, 70.4)
- added IC2: 830S21AMI-01LF, custom_components:SOIC127P600X175-8N, B.Cu at (101.9, 44.0)
- added IC2: 830S21AMI-01LF, custom_components:SOIC127P600X175-8N, B.Cu at (156.4, 42.8)
- added IC2: 830S21AMI-01LF, custom_components:SOIC127P600X175-8N, B.Cu at (129.7, 43.3)
- added IC2: 830S21AMI-01LF, custom_components:SOIC127P600X175-8N, B.Cu at (156.7, 71.4)
- added IC2: 830S21AMI-01LF, custom_components:SOIC127P600X175-8N, B.Cu at (101.9, 73.4)
- added IC2: 830S21AMI-01LF, custom_components:SOIC127P600X175-8N, B.Cu at (128.9, 72.9)
- added R10: 100, Resistor_SMD:R_0603_1608Metric, B.Cu at (102.2, 25.9)
- added R10: 100, Resistor_SMD:R_0603_1608Metric, B.Cu at (156.7, 24.7)
- added R10: 100, Resistor_SMD:R_0603_1608Metric, B.Cu at (129.2, 54.8)
- added R10: 100, Resistor_SMD:R_0603_1608Metric, B.Cu at (156.9, 53.2)
- added R10: 100, Resistor_SMD:R_0603_1608Metric, B.Cu at (102.2, 55.2)
- added R10: 100, Resistor_SMD:R_0603_1608Metric, B.Cu at (129.9, 25.2)
- added R10: 100, Resistor_SMD:R_0603_1608Metric, B.Cu at (182.9, 52.2)
- added R12: 127, Resistor_SMD:R_0603_1608Metric, B.Cu at (162.5, 44.3)
- added R12: 127, Resistor_SMD:R_0603_1608Metric, B.Cu at (188.7, 71.9)
- added R12: 127, Resistor_SMD:R_0603_1608Metric, B.Cu at (108.0, 45.6)
- added R12: 127, Resistor_SMD:R_0603_1608Metric, B.Cu at (135.7, 44.8)
- added R12: 127, Resistor_SMD:R_0603_1608Metric, B.Cu at (135.0, 74.4)
- added R12: 127, Resistor_SMD:R_0603_1608Metric, B.Cu at (108.0, 74.9)
- added R12: 127, Resistor_SMD:R_0603_1608Metric, B.Cu at (162.7, 72.9)
- added R13: 82, Resistor_SMD:R_0603_1608Metric, B.Cu at (161.2, 72.9)
- added R13: 82, Resistor_SMD:R_0603_1608Metric, B.Cu at (161.0, 44.3)
- added R13: 82, Resistor_SMD:R_0603_1608Metric, B.Cu at (106.5, 74.9)
- added R13: 82, Resistor_SMD:R_0603_1608Metric, B.Cu at (133.5, 74.4)
- added R13: 82, Resistor_SMD:R_0603_1608Metric, B.Cu at (187.2, 71.9)
- added R13: 82, Resistor_SMD:R_0603_1608Metric, B.Cu at (134.2, 44.8)
- added R13: 82, Resistor_SMD:R_0603_1608Metric, B.Cu at (106.5, 45.6)
- added R14: 100, Resistor_SMD:R_0603_1608Metric, B.Cu at (108.0, 20.9)
- added R14: 100, Resistor_SMD:R_0603_1608Metric, B.Cu at (162.7, 48.3)
- added R14: 100, Resistor_SMD:R_0603_1608Metric, B.Cu at (162.5, 19.7)
- added R14: 100, Resistor_SMD:R_0603_1608Metric, B.Cu at (135.7, 20.2)
- added R14: 100, Resistor_SMD:R_0603_1608Metric, B.Cu at (108.0, 50.3)
- added R14: 100, Resistor_SMD:R_0603_1608Metric, B.Cu at (188.7, 47.3)
- added R14: 100, Resistor_SMD:R_0603_1608Metric, B.Cu at (135.0, 49.8)
- added R15: 100, Resistor_SMD:R_0603_1608Metric, B.Cu at (190.5, 48.7)
- added R15: 100, Resistor_SMD:R_0603_1608Metric, B.Cu at (164.5, 49.7)
- added R15: 100, Resistor_SMD:R_0603_1608Metric, B.Cu at (109.8, 22.3)
- added R15: 100, Resistor_SMD:R_0603_1608Metric, B.Cu at (164.3, 21.1)
- added R15: 100, Resistor_SMD:R_0603_1608Metric, B.Cu at (109.8, 51.7)
- added R15: 100, Resistor_SMD:R_0603_1608Metric, B.Cu at (137.5, 21.6)
- added R15: 100, Resistor_SMD:R_0603_1608Metric, B.Cu at (136.8, 51.2)
- added R16: 10k, Resistor_SMD:R_0603_1608Metric, B.Cu at (103.2, 60.4)
- added R16: 10k, Resistor_SMD:R_0603_1608Metric, B.Cu at (131.0, 30.3)
- added R16: 10k, Resistor_SMD:R_0603_1608Metric, B.Cu at (103.2, 31.0)
- added R16: 10k, Resistor_SMD:R_0603_1608Metric, B.Cu at (184.0, 57.4)
- added R16: 10k, Resistor_SMD:R_0603_1608Metric, B.Cu at (158.0, 58.4)
- added R16: 10k, Resistor_SMD:R_0603_1608Metric, B.Cu at (157.7, 29.8)
- added R16: 10k, Resistor_SMD:R_0603_1608Metric, B.Cu at (130.2, 59.9)
- added R21: 127, Resistor_SMD:R_0603_1608Metric, B.Cu at (162.7, 69.9)
- added R21: 127, Resistor_SMD:R_0603_1608Metric, B.Cu at (188.7, 68.9)
- added R21: 127, Resistor_SMD:R_0603_1608Metric, B.Cu at (108.0, 42.6)
- added R21: 127, Resistor_SMD:R_0603_1608Metric, B.Cu at (162.5, 41.3)
- added R21: 127, Resistor_SMD:R_0603_1608Metric, B.Cu at (135.7, 41.8)
- added R21: 127, Resistor_SMD:R_0603_1608Metric, B.Cu at (135.0, 71.4)
- added R21: 127, Resistor_SMD:R_0603_1608Metric, B.Cu at (108.0, 71.9)
- added R22: 82, Resistor_SMD:R_0603_1608Metric, B.Cu at (134.2, 41.8)
- added R22: 82, Resistor_SMD:R_0603_1608Metric, B.Cu at (161.0, 41.3)
- added R22: 82, Resistor_SMD:R_0603_1608Metric, B.Cu at (106.5, 71.9)
- added R22: 82, Resistor_SMD:R_0603_1608Metric, B.Cu at (161.2, 69.9)
- added R22: 82, Resistor_SMD:R_0603_1608Metric, B.Cu at (133.5, 71.4)
- added R22: 82, Resistor_SMD:R_0603_1608Metric, B.Cu at (106.5, 42.6)
- added R22: 82, Resistor_SMD:R_0603_1608Metric, B.Cu at (187.2, 68.9)
- added R6: 127, Resistor_SMD:R_0603_1608Metric, F.Cu at (128.3, 40.6)
- added R6: 127, Resistor_SMD:R_0603_1608Metric, F.Cu at (129.4, 71.7)
- added R6: 127, Resistor_SMD:R_0603_1608Metric, F.Cu at (186.3, 41.6)
- added R6: 127, Resistor_SMD:R_0603_1608Metric, F.Cu at (113.0, 40.1)
- added R6: 127, Resistor_SMD:R_0603_1608Metric, F.Cu at (113.7, 72.9)
- added R6: 127, Resistor_SMD:R_0603_1608Metric, F.Cu at (157.3, 41.6)
- added R6: 127, Resistor_SMD:R_0603_1608Metric, F.Cu at (96.7, 73.2)
- added R6: 127, Resistor_SMD:R_0603_1608Metric, F.Cu at (158.7, 73.2)
- added R6: 127, Resistor_SMD:R_0603_1608Metric, F.Cu at (200.3, 41.4)
- added R6: 127, Resistor_SMD:R_0603_1608Metric, F.Cu at (201.9, 73.4)
- added R6: 127, Resistor_SMD:R_0603_1608Metric, F.Cu at (143.0, 40.6)
- added R6: 127, Resistor_SMD:R_0603_1608Metric, F.Cu at (172.9, 73.4)
- added R6: 127, Resistor_SMD:R_0603_1608Metric, F.Cu at (144.4, 72.7)
- added R6: 127, Resistor_SMD:R_0603_1608Metric, F.Cu at (171.8, 41.4)
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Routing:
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- removed copper zone on B.Cu, net /ADC/AGND
- removed copper zone on F.Cu, net /ADC/AGND
- removed copper zone on In1.Cu, net /ADC/AGND
- removed copper zone on In2.Cu, net /ADC/AGND
- removed copper zone on B.Cu, net /ADC/DGND
- removed copper zone on F.Cu, net /ADC/DGND
- removed copper zone on In1.Cu, net /ADC/DGND
- removed copper zone on In2.Cu, net /ADC/DGND
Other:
- board size 110 x 110 mm -> 126 x 79 mm
- board text removed: "1"
- board text removed: "10"
- board text removed: "12"
- board text removed: "13"
- board text removed: "14"
- board text removed: "15"
- board text removed: "16"
- board text removed: "2"
- board text removed: "3"
- board text removed: "4"
- board text removed: "5"
- board text removed: "6"
- board text removed: "7"
- board text removed: "8"
- board text removed: "9"
- board text removed: "Epoxy Here"
